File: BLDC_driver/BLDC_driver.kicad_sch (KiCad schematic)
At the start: 1 part, among them U1 STM32F412CEUx

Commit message: Update
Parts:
- added C1, C3, C4, C5, C6, C8, C9: 100n, Capacitor_SMD:C_0603_1608Metric, symbol Device:C_Small
- added C10, C11: 12p, Capacitor_SMD:C_0603_1608Metric, symbol Device:C_Small
- added C2: 1u, Capacitor_SMD:C_0603_1608Metric, symbol Device:C_Small
- added C7: 4u7, Capacitor_SMD:C_0603_1608Metric, symbol Device:C_Small
- added D1: PWR, LED_SMD:LED_0603_1608Metric, symbol Device:LED
- added D2: STATUS, LED_SMD:LED_0603_1608Metric, symbol Device:LED
- added H1, H2, H3, H4: MountingHole_Pad, MountingHole:MountingHole_3.2mm_M3_Pad_Via, symbol Mechanical:MountingHole_Pad
- added J1: POWER, TerminalBlock:TerminalBlock_Xinya_XY308-2.54-2P_1x02_P2.54mm_Horizontal, symbol Connector:Screw_Terminal_01x02
- added J2: CTRL, Connector_PinHeader_2.00mm:PinHeader_1x04_P2.00mm_Vertical, symbol Connector_Generic:Conn_01x04
- added J4: JTAG, Connector_PinHeader_2.00mm:PinHeader_1x04_P2.00mm_Vertical, symbol Connector_Generic:Conn_01x04
- added L1: 10u, Inductor_SMD:L_0805_2012Metric, symbol Device:L_Small
- added R1: 5k1, Resistor_SMD:R_0603_1608Metric, symbol Device:R_Small
- added R2: 1k, Resistor_SMD:R_0603_1608Metric, symbol Device:R_Small
- added R3, R5: 10k, Resistor_SMD:R_0603_1608Metric, symbol Device:R_Small
- added R4: 47, Resistor_SMD:R_0603_1608Metric, symbol Device:R_Small
- added SW1, SW2: BTN, Button_Switch_SMD:SW_SPST_PTS810, symbol Switch:SW_Push
- added U2: ~, Package_SO:SOIC-8_3.9x4.9mm_P1.27mm, symbol Marijn:AS5600
- added U3: W25Q128JVS, Package_SO:SOIC-8_5.23x5.23mm_P1.27mm, symbol Memory_Flash:W25Q128JVS
- added Y1: 25MHz, Crystal:Crystal_SMD_3225-4Pin_3.2x2.5mm, symbol Device:Crystal_GND24
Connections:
- new net: C11.1, R4.2, Y1.3
- new net: D2.2 (A), R2.2
- new net: D1.2 (A), R1.2
- new net +24V: J1.1 (Pin_1)
- new net +3.3VA: C8.1, L1.2
- new net +3V3: C1.2, C2.1, C3.1, C4.1, C5.1, C6.1, C7.1, J4.1 (Pin_1), L1.1, R1.1, R2.1, R3.1, SW1.2, U2.1 (VDD5), U2.2 (VDD3v3), U3.8 (VCC)
- new net AS5600_OUT: U2.3 (OUT)
- new net BOOT0: R5.1, SW1.1
- new net CTRL_SPI_CLK: J2.3 (Pin_3)
- new net CTRL_SPI_MISO: J2.2 (Pin_2)
- new net CTRL_SPI_MOSI: J2.1 (Pin_1)
- new net CTRL_SPI_NCS: J2.4 (Pin_4)
- new net FLASH_SPI_CLK: U3.6 (CLK)
- new net FLASH_SPI_MISO: U3.2 (DO(IO1))
- new net FLASH_SPI_MOSI: U3.5 (DI(IO0))
- new net FLASH_SPI_NCS: U3.1 (~{CS})
- new net GND: C1.1, C10.2, C11.2, C2.2, C3.2, C4.2, C5.2, C6.2, C7.2, C8.2, C9.1, D1.1 (K), H1.1, H2.1, H3.1, H4.1, J1.2 (Pin_2), J4.4 (Pin_4), R5.2, SW2.2, U2.4 (GND), U2.5 (DIR), U3.4 (GND), Y1.2, Y1.4
- new net HSE_IN: C10.1, Y1.1
- new net HSE_OUT: R4.1
- new net I2C_SCL: U2.6 (SCL)
- new net I2C_SDA: U2.7 (SDA)
- new net JTAG_SWCLK: J4.3 (Pin_3)
- new net JTAG_SWDIO: J4.2 (Pin_2)
- new net NRST: C9.2, R3.2, SW2.1
- new net STATUS: D2.1 (K)
- new net W25Q128_NRST: U3.7 (IO3)
- new net W25Q128_NWP: U3.3 (IO2)
- no-connect marks 0 -> 1
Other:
- added sheet USB (usb.kicad_sch)
- note added: "0x36"
- note added: "Bypass / Filter"
- note added: "Crystal"
- note added: "HAL angle sensor"
- note added: "IO"
- note added: "LED"
- note added: "Mounting"
- note added: "Programming inputs"
- note added: "SPI flash (W25Q128)"
- note added: "USB"

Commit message: Update
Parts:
- removed C1: 100n, Capacitor_SMD:C_0603_1608Metric, symbol Device:C_Small
- removed C2: 1u, Capacitor_SMD:C_0603_1608Metric, symbol Device:C_Small
- removed U2: ~, Package_SO:SOIC-8_3.9x4.9mm_P1.27mm, symbol Marijn:AS5600
- renumbered C3 to C1, C4 to C2, C5 to C3, C6 to C4, C7 to C5, C8 to C6, C9 to C7, C10 to C8, C11 to C9, J4 to J3, U3 to U2
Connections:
- no-connect marks 1 -> 0
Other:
- added sheet phase_logic (phase_logic.kicad_sch)
- note removed: "0x36"
- note removed: "HAL angle sensor"
- moved on the sheet: U2

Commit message: Layout progress
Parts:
- J1: footprint TerminalBlock:TerminalBlock_Xinya_XY308-2.54-2P_1x02_P2.54mm_Horizontal -> Connector_AMASS:AMASS_XT60-F_1x02_P7.20mm_Vertical
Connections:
- net +24V renamed VPWR
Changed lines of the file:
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@@
-	)
-	(symbol
-		(lib_id "power:+24V")
-		(at 146.05 22.86 0)
-		(unit 1)
-		(exclude_from_sim no)
-		(in_bom yes)
-		(on_board yes)
-		(dnp no)
-		(property "Reference" "#PWR03"
-			(at 146.05 26.67 0)
-			(effects
-				(font
-					(size 1.27 1.27)
-				)
-				(hide yes)
-			)
-		)
-		(property "Value" "+24V"
-			(at 144.018 18.796 0)
-			(effects
-				(font
-					(size 1.27 1.27)
-				)
-			)
-		)
-		(property "Footprint" ""
-			(at 146.05 22.86 0)
-			(effects
-				(font
-					(size 1.27 1.27)
-				)
-				(hide yes)
-			)
-		)
-		(property "Datasheet" ""
-			(at 146.05 22.86 0)
-			(effects
-				(font
-					(size 1.27 1.27)
-				)
-				(hide yes)
-			)
-		)
-		(property "Description" "Power symbol creates a global label with name \"+24V\""
-			(at 146.05 22.86 0)
-			(effects
-				(font
-					(size 1.27 1.27)
-				)
-				(hide yes)
-			)
-		)
-		(pin "1"
-		)
-		(instances
-			(project "BLDC_driver"
-				(path "/6f399879-dc45-4210-87b6-ea005f89c132"
-					(reference "#PWR03")
-					(unit 1)
-				)
-			)
-		)
 	)
 	(symbol
@@
 	)
 	(symbol
+		(lib_id "power:Vdrive")
+		(at 146.05 22.86 0)
+		(unit 1)
+		(exclude_from_sim no)
+		(in_bom yes)
+		(on_board yes)
+		(dnp no)
+		(property "Reference" "#PWR03"
+			(at 146.05 26.67 0)
+			(effects
+				(font
+					(size 1.27 1.27)
+				)
+				(hide yes)
+			)
+		)
+		(property "Value" "VPWR"
+			(at 146.05 18.796 0)
+			(effects
+				(font
+					(size 1.27 1.27)
+				)
+			)
+		)
+		(property "Footprint" ""
+			(at 146.05 22.86 0)
+			(effects
+				(font
+					(size 1.27 1.27)
+				)
+				(hide yes)
+			)
+		)
+		(property "Datasheet" ""
+			(at 146.05 22.86 0)
+			(effects
+				(font
+					(size 1.27 1.27)
+				)
+				(hide yes)
+			)
+		)
+		(property "Description" "Power symbol creates a global label with name \"Vdrive\""
+			(at 146.05 22.86 0)
+			(effects
+				(font
+					(size 1.27 1.27)
+				)
+				(hide yes)
+			)
+		)
+		(pin "1"
+		)
+		(instances
+			(project "BLDC_driver"
+				(path "/6f399879-dc45-4210-87b6-ea005f89c132"
+					(reference "#PWR03")
+					(unit 1)
+				)
+			)
+		)
+	)
+	(symbol
 		(lib_id "power:GND")
 		(at 146.05 27.94 0)
@@
 			)
 		)
-		(property "Footprint" "TerminalBlock:TerminalBlock_Xinya_XY308-2.54-2P_1x02_P2.54mm_Horizontal"
+		(property "Footprint" "Connector_AMASS:AMASS_XT60-F_1x02_P7.20mm_Vertical"
 			(at 152.4 24.13 0)
 			(effects

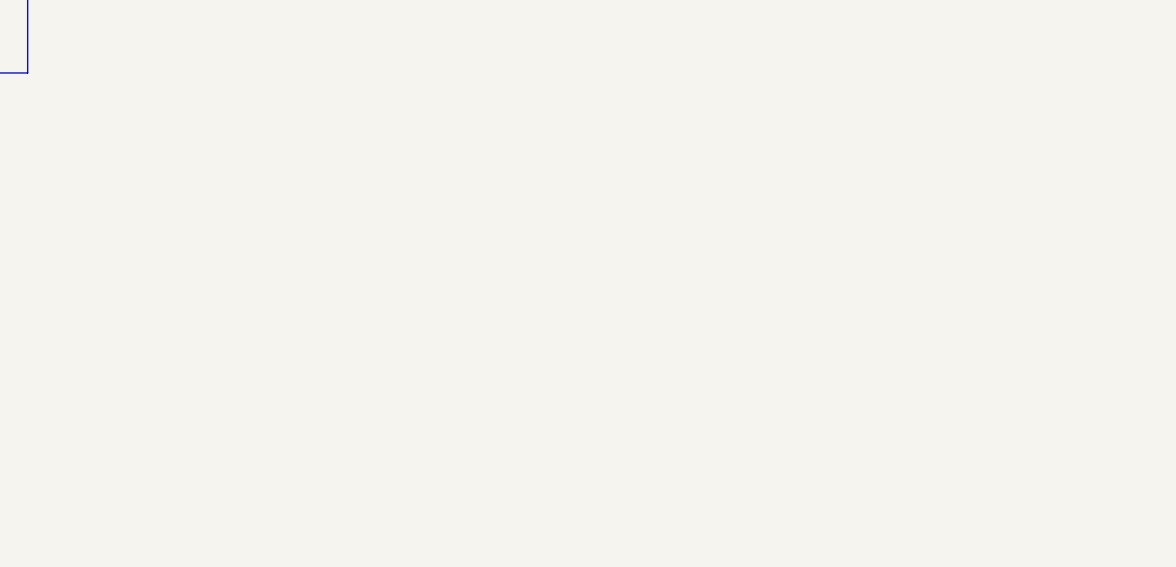
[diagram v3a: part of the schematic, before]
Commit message: Rough inverter stage layout
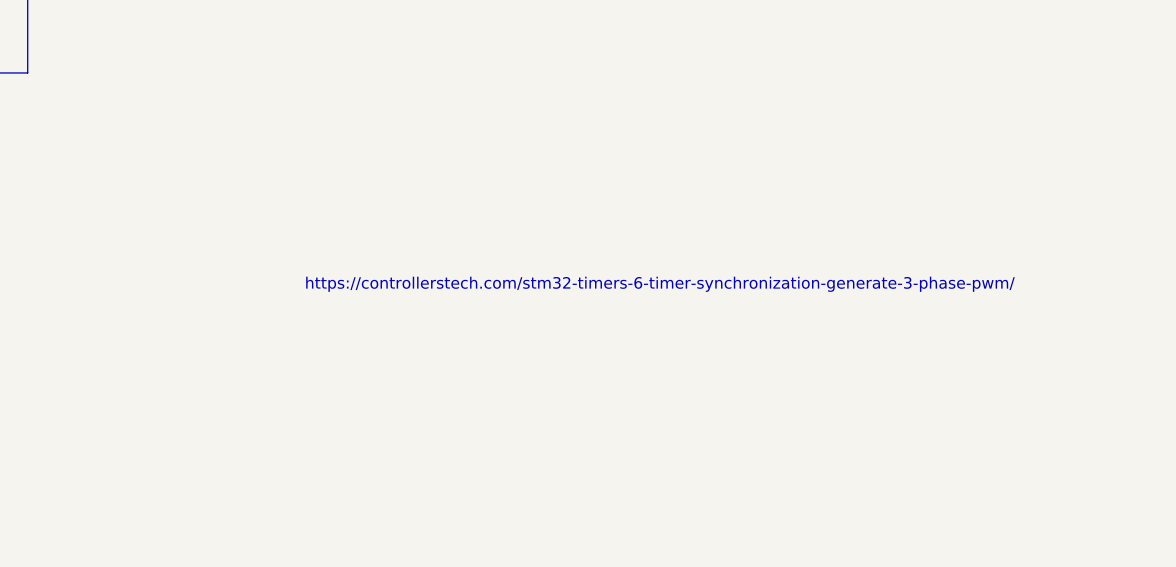
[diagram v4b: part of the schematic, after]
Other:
- note added: "https://controllerstech.com/stm32-timers-6-timer-synchronization-generate-3-phase-pwm/"
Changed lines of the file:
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@@
+		)
+	)
+	(text "https://controllerstech.com/stm32-timers-6-timer-synchronization-generate-3-phase-pwm/"
+		(exclude_from_sim no)
+		(at 224.536 127.762 0)
+		(effects
+			(font
+				(size 1.27 1.27)
+			)
 		)
 	)

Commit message: New design
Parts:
- added C1, C2, C3, C4: 820u/100v, Capacitor_THT:C_Radial_D18.0mm_H35.5mm_P7.50mm, symbol Device:C_Small
- renumbered C6 to C10, C7 to C11, C8 to C12, C9 to C13, C1 to C5, C2 to C6, C3 to C7, C4 to C8, C5 to C9, J2 to J1, J1 to J2
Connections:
- net GND: now also C1.2, C2.2, C3.2, C4.2
- net VPWR: now also C1.1, C2.1, C3.1, C4.1
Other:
- sheet phase_logic renamed inverter stage
- sheet inverter stage: file phase_logic.kicad_sch -> inverter_stage.kicad_sch
- note added: "Inverter stage"
- moved on the sheet: J2

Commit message: Layout progress
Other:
- added sheet power (power.kicad_sch)
- note added: "Power"
- note added: "Power connector"
- note added: "TODO"
- moved on the sheet: C1, C2, C3, C4, J2

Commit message: Layout progress
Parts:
- removed H1, H2, H3, H4: MountingHole_Pad, MountingHole:MountingHole_3.2mm_M3_Pad_Via, symbol Mechanical:MountingHole_Pad
- added C5, C6, C7, C8: 2u2/100v, Capacitor_SMD:C_1210_3225Metric, symbol Device:C_Small
- renumbered C6 to C10, C7 to C11, C8 to C12, C9 to C13, C10 to C14, C11 to C15, C12 to C16, C13 to C17, C5 to C9
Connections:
- net GND: now also C5.2, C6.2, C7.2, C8.2
- net VPWR: now also C5.1, C6.1, C7.1, C8.1
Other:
- note removed: "Mounting"
- moved on the sheet: C1, C2, C3, C4, D1, D2, J1, J2, R1, R2

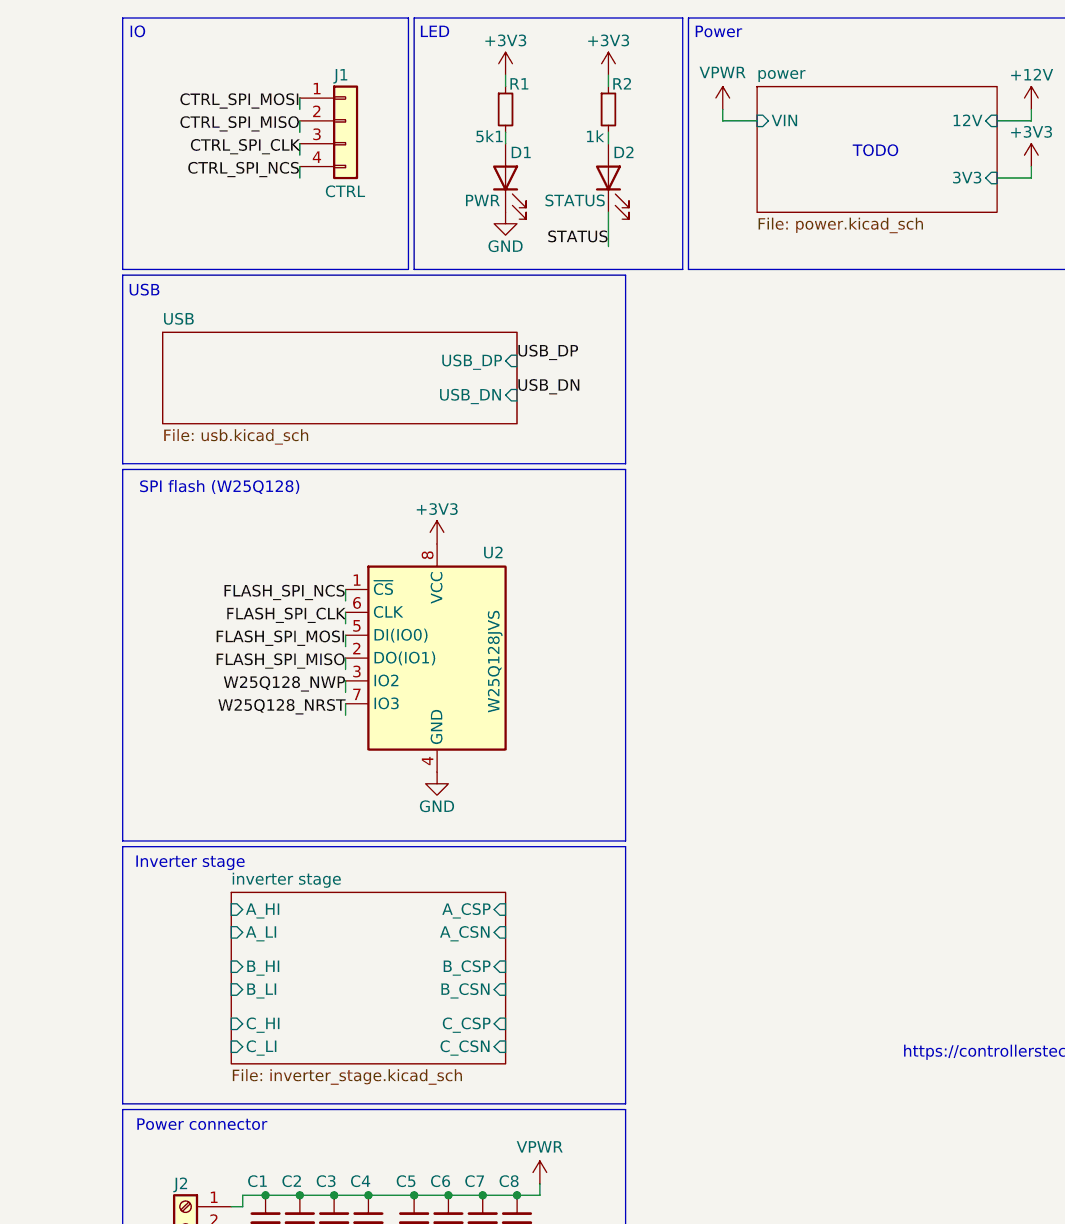
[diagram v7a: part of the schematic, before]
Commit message: Started on power conversion section
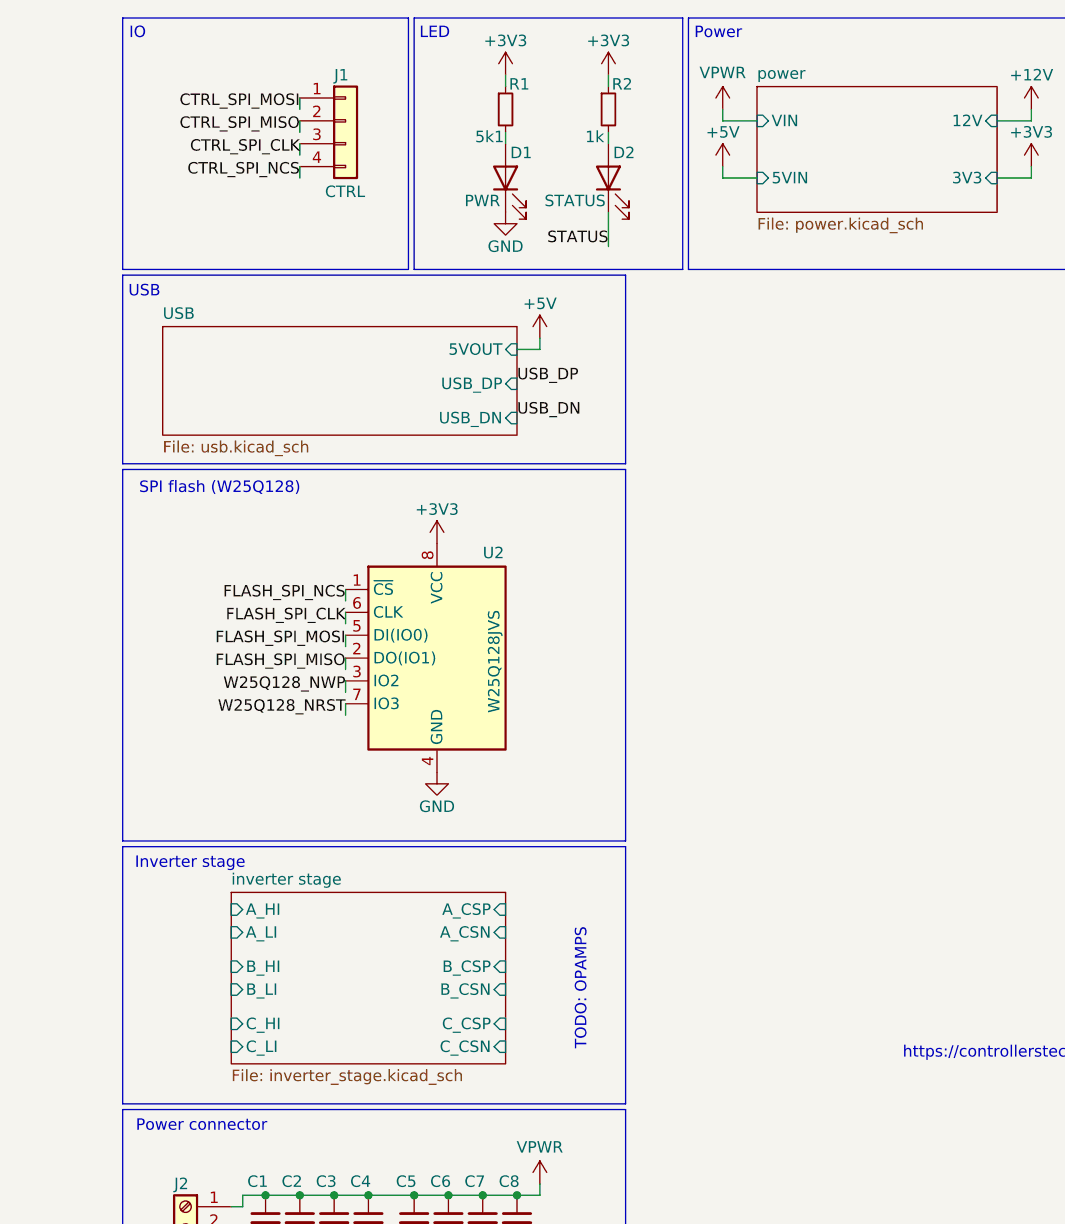
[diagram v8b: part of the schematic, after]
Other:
- sheet USB ports: added 5VOUT; removed none
- sheet power ports: added 5VIN; removed none
- note added: "TODO: OPAMPS"
- note removed: "TODO"
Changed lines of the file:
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@@
 	(wire
 		(pts
+			(xy 144.78 49.53) (xy 142.24 49.53)
+		)
+		(stroke
+			(width 0)
+			(type default)
+		)
+	)
+	(wire
+		(pts
 			(xy 67.31 176.53) (xy 67.31 177.8)
 		)
@@
 	(wire
 		(pts
+			(xy 165.1 29.21) (xy 165.1 30.48)
+		)
+		(stroke
+			(width 0)
+			(type default)
+		)
+	)
+	(wire
+		(pts
 			(xy 135.89 175.26) (xy 144.78 175.26)
 		)
@@
 	(wire
 		(pts
+			(xy 165.1 30.48) (xy 168.91 30.48)
+		)
+		(stroke
+			(width 0)
+			(type default)
+		)
+	)
+	(wire
+		(pts
 			(xy 111.76 143.51) (xy 114.3 143.51)
 		)
@@
 	(wire
 		(pts
+			(xy 144.78 48.26) (xy 144.78 49.53)
+		)
+		(stroke
+			(width 0)
+			(type default)
+		)
+	)
+	(wire
+		(pts
 			(xy 130.81 148.59) (xy 134.62 148.59)
 		)
@@
 		)
 	)
+	(text "TODO: OPAMPS"
+		(exclude_from_sim no)
+		(at 149.352 120.65 90)
+		(effects
+			(font
+				(size 1.27 1.27)
+			)
+		)
+	)
 	(text "https://controllerstech.com/stm32-timers-6-timer-synchronization-generate-3-phase-pwm/"
 		(exclude_from_sim no)
@@
 		)
 	)
-	(text "TODO"
-		(exclude_from_sim no)
-		(at 182.118 27.686 0)
-		(effects
-			(font
-				(size 1.27 1.27)
-			)
-		)
-	)
 	(text "USB"
 		(exclude_from_sim no)
@@
 	)
 	(label "USB_DP"
-		(at 142.24 50.8 0)
+		(at 142.24 53.34 0)
 		(fields_autoplaced yes)
 		(effects
@@
 	)
 	(label "USB_DN"
-		(at 142.24 54.61 0)
+		(at 142.24 57.15 0)
 		(fields_autoplaced yes)
 		(effects
@@
 	)
 	(symbol
+		(lib_id "power:+5V")
+		(at 144.78 48.26 0)
+		(unit 1)
+		(exclude_from_sim no)
+		(in_bom yes)
+		(on_board yes)
+		(dnp no)
+		(property "Reference" "#PWR058"
+			(at 144.78 52.07 0)
+			(effects
+				(font
+					(size 1.27 1.27)
+				)
+				(hide yes)
+			)
+		)
+		(property "Value" "+5V"
+			(at 144.78 44.45 0)
+			(effects
+				(font
+					(size 1.27 1.27)
+				)
+			)
+		)
+		(property "Footprint" ""
+			(at 144.78 48.26 0)
+			(effects
+				(font
+					(size 1.27 1.27)
+				)
+				(hide yes)
+			)
+		)
+		(property "Datasheet" ""
+			(at 144.78 48.26 0)
+			(effects
+				(font
+					(size 1.27 1.27)
+				)
+				(hide yes)
+			)
+		)
+		(property "Description" "Power symbol creates a global label with name \"+5V\""
+			(at 144.78 48.26 0)
+			(effects
+				(font
+					(size 1.27 1.27)
+				)
+				(hide yes)
+			)
+		)
+		(pin "1"
+		)
+		(instances
+			(project "BLDC_driver"
+				(path "/6f399879-dc45-4210-87b6-ea005f89c132"
+					(reference "#PWR058")
+					(unit 1)
+				)
+			)
+		)
+	)
+	(symbol
 		(lib_id "Device:C_Small")
 		(at 138.43 146.05 0)
@@
 	)
 	(symbol
+		(lib_id "power:+5V")
+		(at 165.1 29.21 0)
+		(unit 1)
+		(exclude_from_sim no)
+		(in_bom yes)
+		(on_board yes)
+		(dnp no)
+		(property "Reference" "#PWR056"
+			(at 165.1 33.02 0)
+			(effects
+				(font
+					(size 1.27 1.27)
+				)
+				(hide yes)
+			)
+		)
+		(property "Value" "+5V"
+			(at 165.1 25.4 0)
+			(effects
+				(font
+					(size 1.27 1.27)
+				)
+			)
+		)
+		(property "Footprint" ""
+			(at 165.1 29.21 0)
+			(effects
+				(font
+					(size 1.27 1.27)
+				)
+				(hide yes)
+			)
+		)
+		(property "Datasheet" ""
+			(at 165.1 29.21 0)
+			(effects
+				(font
+					(size 1.27 1.27)
+				)
+				(hide yes)
+			)
+		)
+		(property "Description" "Power symbol creates a global label with name \"+5V\""
+			(at 165.1 29.21 0)
+			(effects
+				(font
+					(size 1.27 1.27)
+				)
+				(hide yes)
+			)
+		)
+		(pin "1"
+		)
+		(instances
+			(project ""
+				(path "/6f399879-dc45-4210-87b6-ea005f89c132"
+					(reference "#PWR056")
+					(unit 1)
+				)
+			)
+		)
+	)
+	(symbol
 		(lib_id "Device:C_Small")
 		(at 114.3 146.05 0)
@@
 	)
 	(sheet
-		(at 102.87 47.625)
-		(size 39.37 10.16)
+		(at 102.87 46.99)
+		(size 39.37 12.065)
 		(fields_autoplaced yes)
 		(stroke
@@
 		)
 		(property "Sheetname" "USB"
-			(at 102.87 46.9134 0)
+			(at 102.87 46.2784 0)
 			(effects
 				(font
@@
 		)
 		(property "Sheetfile" "usb.kicad_sch"
-			(at 102.87 58.3696 0)
+			(at 102.87 59.6396 0)
 			(effects
 				(font
@@
 		)
 		(pin "USB_DP" input
-			(at 142.24 50.8 0)
+			(at 142.24 53.34 0)
 			(effects
 				(font
@@
 		)
 		(pin "USB_DN" input
-			(at 142.24 54.61 0)
+			(at 142.24 57.15 0)
+			(effects
+				(font
+					(size 1.27 1.27)
+				)
+				(justify right)
+			)
+		)
+		(pin "5VOUT" input
+			(at 142.24 49.53 0)
 			(effects
 				(font
@@
 			(effects
 				(font
+					(size 1.27 1.27)
+				)
+				(justify left)
+			)
+		)
+		(pin "5VIN" input
+			(at 168.91 30.48 180)
+			(effects
+				(font
